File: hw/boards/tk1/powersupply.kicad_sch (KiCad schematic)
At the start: 19 parts, among them U1 MCP1824T-2502EOT, U2 MIC5258-1.2YM5, U9 NCP752BSN33T1G

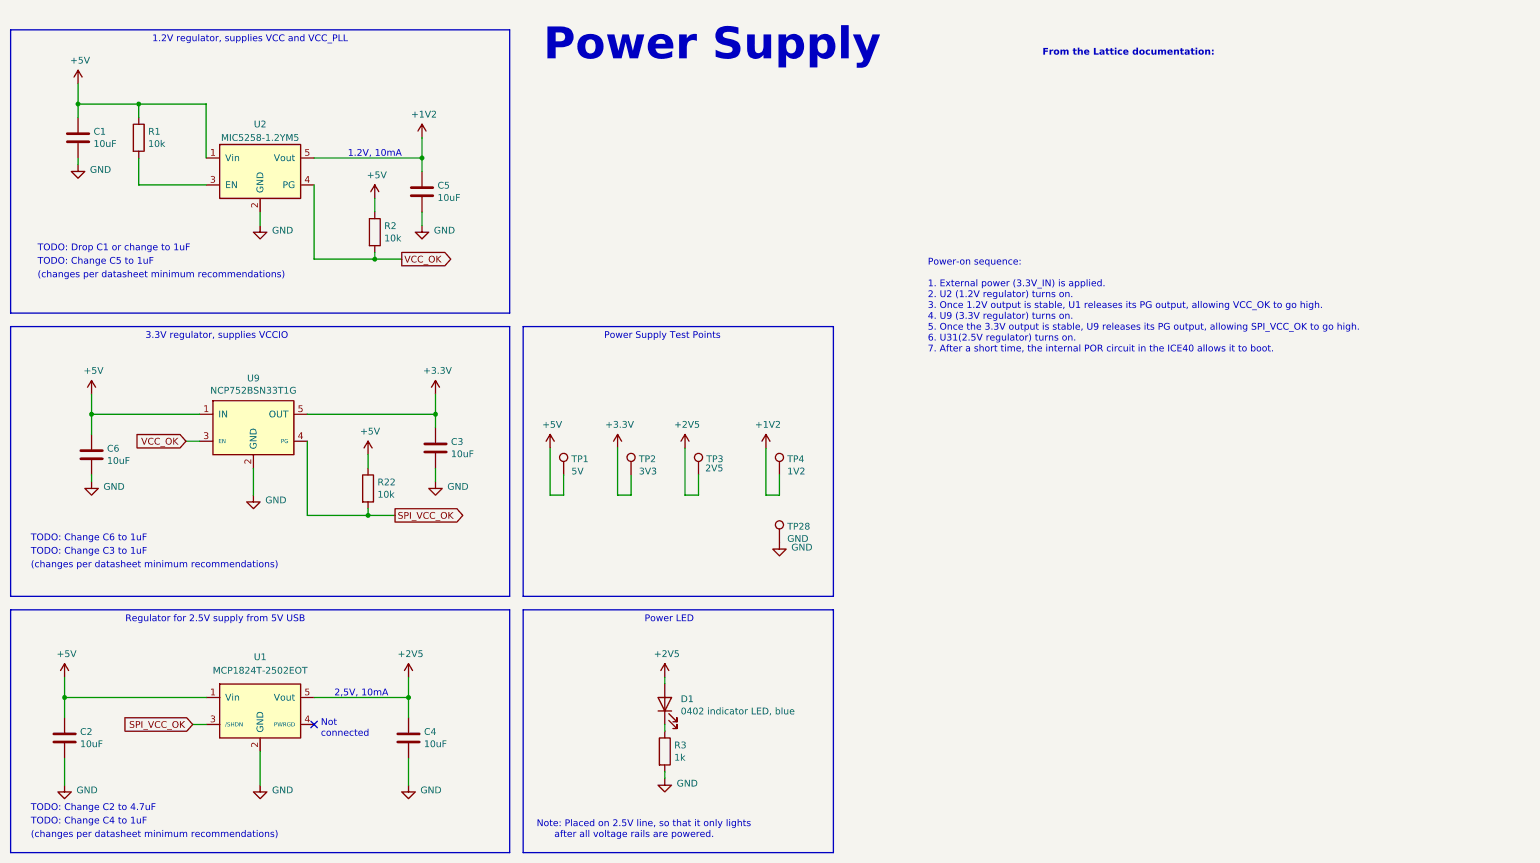
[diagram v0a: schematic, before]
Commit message: Update component values for TK1 PCB
* Use specific part # for C8
* Change flash back to Winbond part, for easier sourcing
* Change C1 to 1pF
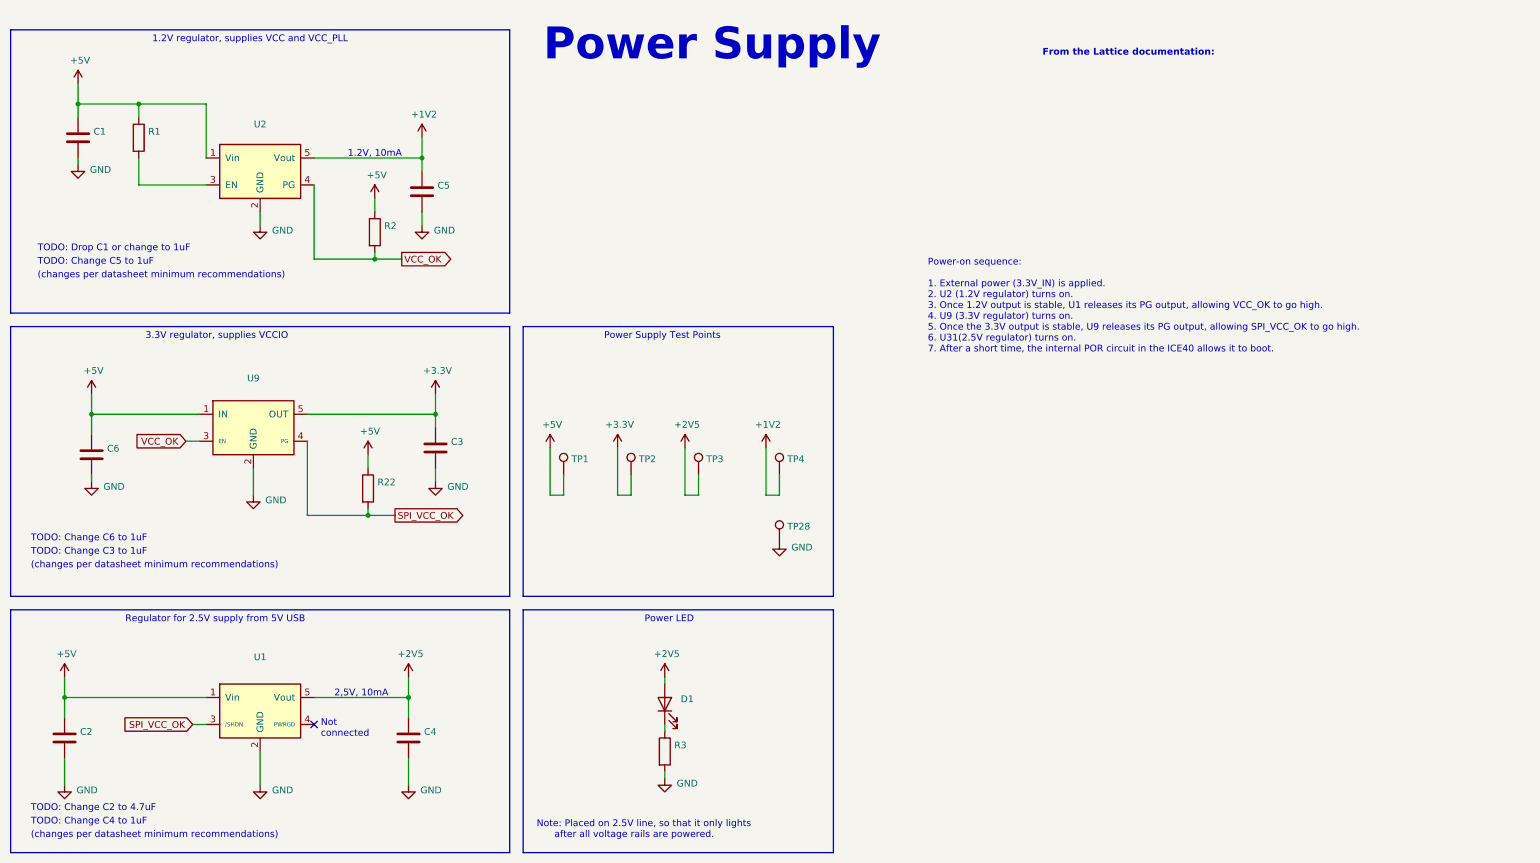
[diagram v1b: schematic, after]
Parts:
- C1, C2, C3, C4, C5, C6: value 10uF -> (none); footprint mta1:CAPC1608X09L -> (none)
- D1: value 0402 indicator LED, blue -> (none); footprint LED_SMD:LED_0402_1005Metric -> (none)
- R1, R2, R22: value 10k -> (none); footprint mta1:ERJ2G(0402)_L -> (none)
- R3: value 1k -> (none); footprint mta1:ERJ2G(0402)_L -> (none)
- TP1: value 5V -> (none); footprint TestPoint:TestPoint_Pad_D1.0mm -> (none)
- TP2: value 3V3 -> (none); footprint TestPoint:TestPoint_Pad_D1.0mm -> (none)
- TP28: value GND -> (none); footprint TestPoint:TestPoint_Pad_D1.0mm -> (none)
- TP3: value 2V5 -> (none); footprint TestPoint:TestPoint_Pad_D1.0mm -> (none)
- TP4: value 1V2 -> (none); footprint TestPoint:TestPoint_Pad_D1.0mm -> (none)
- U1: value MCP1824T-2502EOT -> (none)
- U2: value MIC5258-1.2YM5 -> (none)
- U9: value NCP752BSN33T1G -> (none); footprint mta1:NCP752BSN33T1G -> (none)
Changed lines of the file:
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@@
       (effects (font (size 1.27 1.27)) (justify left))
     )
-    (property "Value" "10uF" (id 1) (at 33.401 39.243 0)
-      (effects (font (size 1.27 1.27)) (justify left))
-    )
-    (property "Footprint" "mta1:CAPC1608X09L" (id 2) (at 31.4452 41.91 0)
+    (property "Value" "" (id 1) (at 33.401 39.243 0)
+      (effects (font (size 1.27 1.27)) (justify left))
+    )
+    (property "Footprint" "" (id 2) (at 31.4452 41.91 0)
       (effects (font (size 1.27 1.27)) hide)
     )
@@
       (effects (font (size 1.27 1.27)) (justify left))
     )
-    (property "Value" "10k" (id 1) (at 43.688 39.243 0)
-      (effects (font (size 1.27 1.27)) (justify left))
-    )
-    (property "Footprint" "mta1:ERJ2G(0402)_L" (id 2) (at 40.132 38.1 90)
+    (property "Value" "" (id 1) (at 43.688 39.243 0)
+      (effects (font (size 1.27 1.27)) (justify left))
+    )
+    (property "Footprint" "" (id 2) (at 40.132 38.1 90)
       (effects (font (size 1.27 1.27)) hide)
     )
@@
       (effects (font (size 1.27 1.27)) (justify left))
     )
-    (property "Value" "10uF" (id 1) (at 98.171 49.403 0)
-      (effects (font (size 1.27 1.27)) (justify left))
-    )
-    (property "Footprint" "mta1:CAPC1608X09L" (id 2) (at 96.2152 52.07 0)
+    (property "Value" "" (id 1) (at 98.171 49.403 0)
+      (effects (font (size 1.27 1.27)) (justify left))
+    )
+    (property "Footprint" "" (id 2) (at 96.2152 52.07 0)
       (effects (font (size 1.27 1.27)) hide)
     )
@@
       (effects (font (size 1.27 1.27)) (justify left))
     )
-    (property "Value" "10k" (id 1) (at 88.138 57.023 0)
-      (effects (font (size 1.27 1.27)) (justify left))
-    )
-    (property "Footprint" "mta1:ERJ2G(0402)_L" (id 2) (at 84.582 55.88 90)
+    (property "Value" "" (id 1) (at 88.138 57.023 0)
+      (effects (font (size 1.27 1.27)) (justify left))
+    )
+    (property "Footprint" "" (id 2) (at 84.582 55.88 90)
       (effects (font (size 1.27 1.27)) hide)
     )
@@
       (effects (font (size 1.27 1.27)) (justify left))
     )
-    (property "Value" "10uF" (id 1) (at 100.711 97.663 0)
-      (effects (font (size 1.27 1.27)) (justify left))
-    )
-    (property "Footprint" "mta1:CAPC1608X09L" (id 2) (at 98.7552 100.33 0)
+    (property "Value" "" (id 1) (at 100.711 97.663 0)
+      (effects (font (size 1.27 1.27)) (justify left))
+    )
+    (property "Footprint" "" (id 2) (at 98.7552 100.33 0)
       (effects (font (size 1.27 1.27)) hide)
     )
@@
     (in_bom yes) (on_board yes)
     (property "Reference" "U2" (id 0) (at 64.77 35.56 0))
-    (property "Value" "MIC5258-1.2YM5" (id 1) (at 64.77 38.1 0))
+    (property "Value" "" (id 1) (at 64.77 38.1 0))
     (property "Footprint" "Package_TO_SOT_SMD:SOT-23-5" (id 2) (at 64.77 34.29 0)
       (effects (font (size 1.27 1.27)) hide)
@@
     (in_bom yes) (on_board yes)
     (property "Reference" "U1" (id 0) (at 64.77 135.89 0))
-    (property "Value" "MCP1824T-2502EOT" (id 1) (at 64.77 138.43 0))
+    (property "Value" "" (id 1) (at 64.77 138.43 0))
     (property "Footprint" "Package_TO_SOT_SMD:SOT-23-5" (id 2) (at 83.82 156.21 0)
       (effects (font (size 1.27 1.27)) hide)
@@
       (effects (font (size 1.27 1.27)) (justify left))
     )
-    (property "Value" "10uF" (id 1) (at 30.861 152.273 0)
-      (effects (font (size 1.27 1.27)) (justify left))
-    )
-    (property "Footprint" "mta1:CAPC1608X09L" (id 2) (at 28.9052 154.94 0)
+    (property "Value" "" (id 1) (at 30.861 152.273 0)
+      (effects (font (size 1.27 1.27)) (justify left))
+    )
+    (property "Footprint" "" (id 2) (at 28.9052 154.94 0)
       (effects (font (size 1.27 1.27)) hide)
     )
@@
       (effects (font (size 1.27 1.27)) (justify left))
     )
-    (property "Value" "10uF" (id 1) (at 95.631 152.273 0)
-      (effects (font (size 1.27 1.27)) (justify left))
-    )
-    (property "Footprint" "mta1:CAPC1608X09L" (id 2) (at 93.6752 154.94 0)
+    (property "Value" "" (id 1) (at 95.631 152.273 0)
+      (effects (font (size 1.27 1.27)) (justify left))
+    )
+    (property "Footprint" "" (id 2) (at 93.6752 154.94 0)
       (effects (font (size 1.27 1.27)) hide)
     )
@@
       (effects (font (size 1.27 1.27)) (justify left))
     )
-    (property "Value" "3V3" (id 1) (at 136.0932 100.9142 0)
-      (effects (font (size 1.27 1.27)) (justify left))
-    )
-    (property "Footprint" "TestPoint:TestPoint_Pad_D1.0mm" (id 2) (at 139.7 101.6 0)
+    (property "Value" "" (id 1) (at 136.0932 100.9142 0)
+      (effects (font (size 1.27 1.27)) (justify left))
+    )
+    (property "Footprint" "" (id 2) (at 139.7 101.6 0)
       (effects (font (size 1.27 1.27)) hide)
     )
@@
       (effects (font (size 1.27 1.27)) (justify left))
     )
-    (property "Value" "2V5" (id 1) (at 148.59 100.33 0)
-      (effects (font (size 1.27 1.27)) (justify left))
-    )
-    (property "Footprint" "TestPoint:TestPoint_Pad_D1.0mm" (id 2) (at 152.4 101.6 0)
+    (property "Value" "" (id 1) (at 148.59 100.33 0)
+      (effects (font (size 1.27 1.27)) (justify left))
+    )
+    (property "Footprint" "" (id 2) (at 152.4 101.6 0)
       (effects (font (size 1.27 1.27)) hide)
     )
@@
       (effects (font (size 1.27 1.27)) (justify left))
     )
-    (property "Value" "1V2" (id 1) (at 164.0332 100.9142 0)
-      (effects (font (size 1.27 1.27)) (justify left))
-    )
-    (property "Footprint" "TestPoint:TestPoint_Pad_D1.0mm" (id 2) (at 167.64 101.6 0)
+    (property "Value" "" (id 1) (at 164.0332 100.9142 0)
+      (effects (font (size 1.27 1.27)) (justify left))
+    )
+    (property "Footprint" "" (id 2) (at 167.64 101.6 0)
       (effects (font (size 1.27 1.27)) hide)
     )
@@
     (in_bom yes) (on_board yes)
     (property "Reference" "U9" (id 0) (at 63.5 83.3882 0))
-    (property "Value" "NCP752BSN33T1G" (id 1) (at 63.5 85.6996 0))
-    (property "Footprint" "mta1:NCP752BSN33T1G" (id 2) (at 63.5 83.82 0)
+    (property "Value" "" (id 1) (at 63.5 85.6996 0))
+    (property "Footprint" "" (id 2) (at 63.5 83.82 0)
       (effects (font (size 1.27 1.27)) hide)
     )
@@
       (effects (font (size 1.27 1.27)) (justify left))
     )
-    (property "Value" "10uF" (id 1) (at 35.941 98.933 0)
-      (effects (font (size 1.27 1.27)) (justify left))
-    )
-    (property "Footprint" "mta1:CAPC1608X09L" (id 2) (at 33.9852 101.6 0)
+    (property "Value" "" (id 1) (at 35.941 98.933 0)
+      (effects (font (size 1.27 1.27)) (justify left))
+    )
+    (property "Footprint" "" (id 2) (at 33.9852 101.6 0)
       (effects (font (size 1.27 1.27)) hide)
     )
@@
       (effects (font (size 1.27 1.27)) (justify left))
     )
-    (property "Value" "1k" (id 1) (at 142.748 154.813 0)
-      (effects (font (size 1.27 1.27)) (justify left))
-    )
-    (property "Footprint" "mta1:ERJ2G(0402)_L" (id 2) (at 139.192 153.67 90)
+    (property "Value" "" (id 1) (at 142.748 154.813 0)
+      (effects (font (size 1.27 1.27)) (justify left))
+    )
+    (property "Footprint" "" (id 2) (at 139.192 153.67 90)
       (effects (font (size 1.27 1.27)) hide)
     )
@@
       (effects (font (size 1.27 1.27)) (justify right))
     )
-    (property "Value" "0402 indicator LED, blue" (id 1) (at 143.9672 146.1008 90)
+    (property "Value" "" (id 1) (at 143.9672 146.1008 90)
       (effects (font (size 1.27 1.27)) (justify right))
     )
-    (property "Footprint" "LED_SMD:LED_0402_1005Metric" (id 2) (at 140.97 144.78 0)
+    (property "Footprint" "" (id 2) (at 140.97 144.78 0)
       (effects (font (size 1.27 1.27)) hide)
     )
@@
       (effects (font (size 1.27 1.27)) (justify left))
     )
-    (property "Value" "5V" (id 1) (at 123.3932 100.9142 0)
-      (effects (font (size 1.27 1.27)) (justify left))
-    )
-    (property "Footprint" "TestPoint:TestPoint_Pad_D1.0mm" (id 2) (at 127 101.6 0)
+    (property "Value" "" (id 1) (at 123.3932 100.9142 0)
+      (effects (font (size 1.27 1.27)) (justify left))
+    )
+    (property "Footprint" "" (id 2) (at 127 101.6 0)
       (effects (font (size 1.27 1.27)) hide)
     )
@@
       (effects (font (size 1.27 1.27)) (justify left))
     )
-    (property "Value" "10k" (id 1) (at 86.868 105.283 0)
-      (effects (font (size 1.27 1.27)) (justify left))
-    )
-    (property "Footprint" "mta1:ERJ2G(0402)_L" (id 2) (at 83.312 104.14 90)
+    (property "Value" "" (id 1) (at 86.868 105.283 0)
+      (effects (font (size 1.27 1.27)) (justify left))
+    )
+    (property "Footprint" "" (id 2) (at 83.312 104.14 90)
       (effects (font (size 1.27 1.27)) hide)
     )
@@
       (effects (font (size 1.27 1.27)) (justify left))
     )
-    (property "Value" "GND" (id 1) (at 164.0332 113.6142 0)
-      (effects (font (size 1.27 1.27)) (justify left))
-    )
-    (property "Footprint" "TestPoint:TestPoint_Pad_D1.0mm" (id 2) (at 167.64 114.3 0)
-      (effects (font (size 1.27 1.27)) hide)
-    )
+    (property "Value" "" (id 1) (at 164.0332 113.6142 0)
+      (effects (font (size 1.27 1.27)) (justify left))
+    )
+    (property "Footprint" "" (id 2) (at 167.64 114.3 0)
+      (effects (font (size 1.27 1.27)) hide)
+    )
